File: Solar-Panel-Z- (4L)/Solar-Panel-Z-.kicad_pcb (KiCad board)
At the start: 4 copper layers, 48.4 x 48.4 mm, 89 parts, among them J1 FTS-105-01-X-DV-A, J2 U.FL-R-SMT-1, Q1 NX3008NBKS, Q2 MBT2222ADW1T1, Q3 NX3008NBKS, Q4 MBT2222ADW1T1, Q5 IRLML2803, Q6 IRF7404, U1 BQ25570RGRR, U2 OPT3001, U3 ATB2012-50011-T000, U4 MAX40200AUK

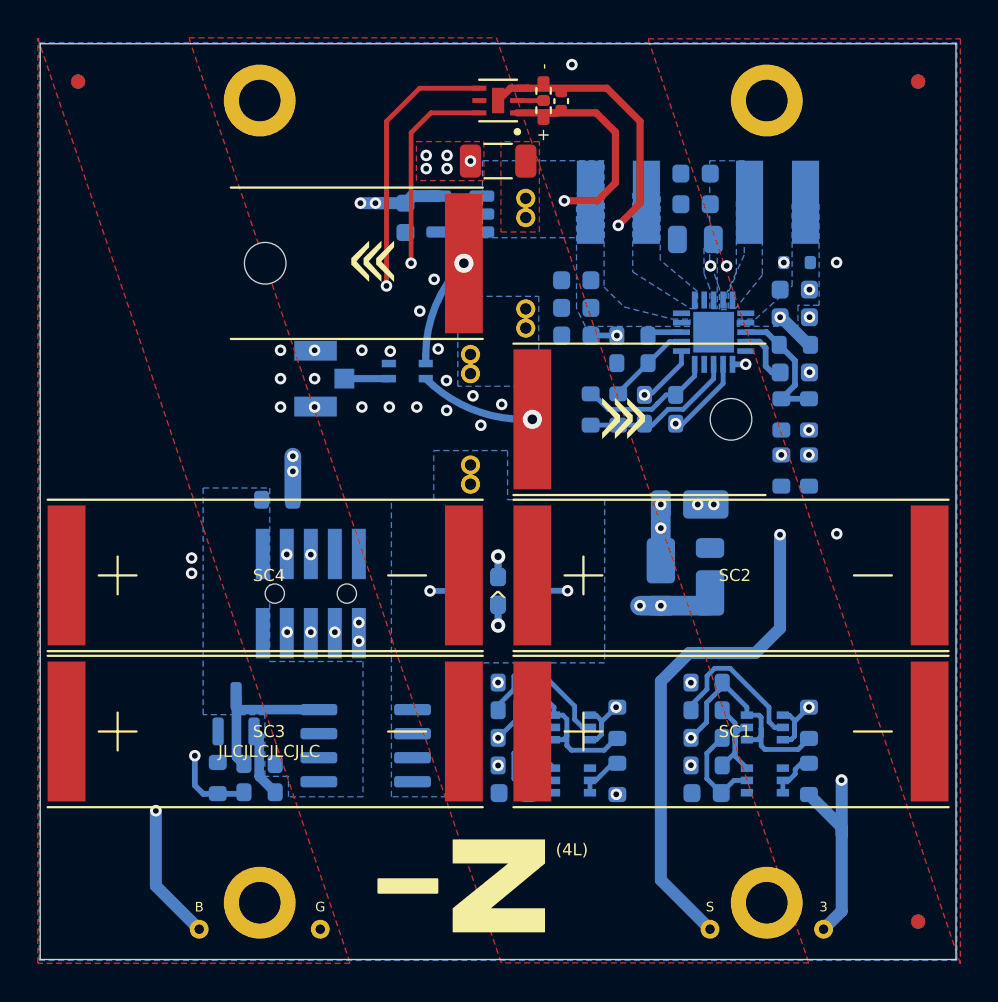
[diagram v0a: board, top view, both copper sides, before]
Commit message: Updated Mounting Holes
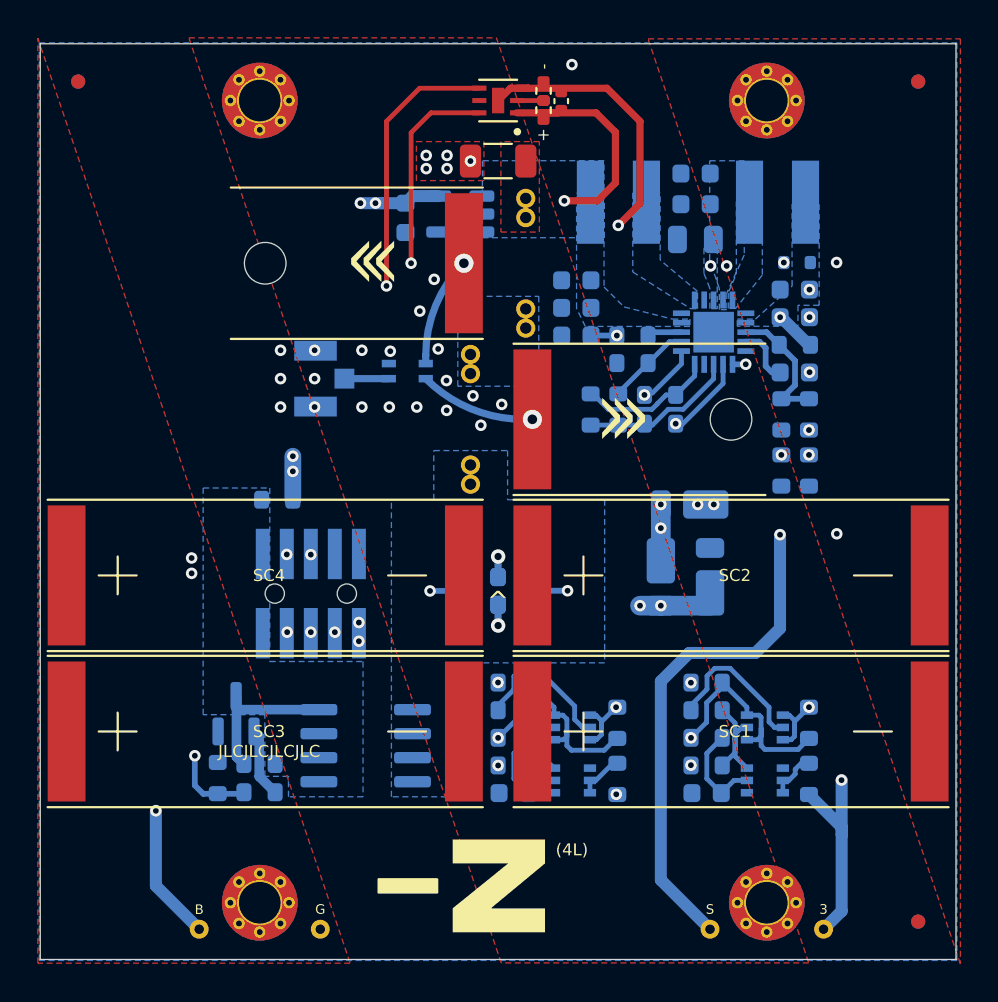
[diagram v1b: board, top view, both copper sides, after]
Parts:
- H1, H2, H3, H4: footprint MountingHole:MountingHole_2.2mm_M2_DIN965_Pad -> solarpanels:MountingHole_2.2mm_M2_DIN965_Pad_TopBottom; moved to F.Cu
- turned H1 to 0 degrees
- turned H2 to 0 degrees
- turned H3 to 0 degrees
- turned H4 to 0 degrees

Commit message: B3/02 Updates
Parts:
- C1: value 1uF -> 0.1uF
- JP1, JP2: moved to F.Cu
- turned JP1 to 180 degrees
- turned JP2 to 180 degrees
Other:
- board text added: "Rev B3/02"
- board text removed: "Rev B3/01"

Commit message: Minor Fixes
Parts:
- JP1: value BurnWire 1 -> BurnWire
- JP2: value BurnWire 2 -> BurnWire
- renumbered U3 to BA1, R32 to R31, R33 to R32, R34 to R33, R35 to R34, U4 to U3
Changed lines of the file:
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@@
   (net 34 "Net-(Q2A-B1)")
   (net 35 "VBAT")
-  (net 36 "Net-(H5-Pad1)")
-  (net 37 "Net-(H6-Pad1)")
+  (net 36 "Net-(BA1-Pad3)")
+  (net 37 "Net-(BA1-Pad4)")
   (net 38 "Net-(Q3A-G2)")
   (net 39 "/VBURN")
@@
   (net 44 "Net-(U2-ADDR)")
   (net 45 "unconnected-(U2-INT-Pad5)")
-  (net 46 "unconnected-(U4-NC-Pad4)")
+  (net 46 "unconnected-(U3-NC-Pad4)")
   (net 47 "Net-(JP2-Pad2)")
   (footprint "solarpanels:KXOB25-05X3F" (layer "F.Cu")
@@
     (property "ki_keywords" "R res resistor")
     (attr smd)
-    (fp_text reference "R35" (at 0 -1.82) (layer "F.SilkS") hide
+    (fp_text reference "R34" (at 0 -1.82) (layer "F.SilkS") hide
         (effects (font (size 1 1) (thickness 0.15)))
     )
@@
         (effects (font (size 0.635 0.635) (thickness 0.1016)))
     )
-    (fp_text value "BurnWire 1" (at 0 4.826) (layer "F.Fab")
+    (fp_text value "BurnWire" (at 0 4.826) (layer "F.Fab")
         (effects (font (size 0.635 0.635) (thickness 0.1016)))
     )
@@
         (effects (font (size 0.635 0.635) (thickness 0.1016)))
     )
-    (fp_text value "BurnWire 2" (at 0 4.826) (layer "F.Fab")
+    (fp_text value "BurnWire" (at 0 4.826) (layer "F.Fab")
         (effects (font (size 0.635 0.635) (thickness 0.1016)))
     )
@@
     (pad "" np_thru_hole circle (at 10.5 0 180) (size 2.2 2.2) (drill 2.2) (layers "F&B.Cu" "*.Mask"))
     (pad "1" smd rect (at 0 0 180) (size 2 7.4) (layers "F.Cu" "F.Paste" "F.Mask")
-      (net 37 "Net-(H6-Pad1)") (pinfunction "1") (pintype "input"))
+      (net 36 "Net-(BA1-Pad3)") (pinfunction "1") (pintype "input"))
   )
   (footprint "Fiducial:Fiducial_0.75mm_Mask1.5mm" (layer "F.Cu")
@@
     (pad "" np_thru_hole circle (at 10.5 0) (size 2.2 2.2) (drill 2.2) (layers "F&B.Cu" "*.Mask"))
     (pad "1" smd rect (at 0 0) (size 2 7.4) (layers "F.Cu" "F.Paste" "F.Mask")
-      (net 36 "Net-(H5-Pad1)") (pinfunction "1") (pintype "input"))
+      (net 37 "Net-(BA1-Pad4)") (pinfunction "1") (pintype "input"))
   )
   (footprint "solarpanels:OPT3001" (layer "F.Cu")
@@
     (property "ki_keywords" "balun rf transformer")
     (attr smd)
-    (fp_text reference "U3" (at 0 0 unlocked) (layer "B.SilkS")
+    (fp_text reference "BA1" (at 0 0 unlocked) (layer "B.SilkS")
         (effects (font (size 0.381 0.381) (thickness 0.0762)) (justify mirror))
     )
@@
       (net 1 "GND") (pinfunction "GND") (pintype "power_in"))
     (pad "3" smd rect (at 0.975 -0.4) (size 0.75 0.4) (layers "B.Cu" "B.Paste" "B.Mask")
-      (net 37 "Net-(H6-Pad1)") (pintype "passive"))
+      (net 36 "Net-(BA1-Pad3)") (pintype "passive"))
     (pad "4" smd rect (at 0.975 0.4) (size 0.75 0.4) (layers "B.Cu" "B.Paste" "B.Mask")
-      (net 36 "Net-(H5-Pad1)") (pintype "passive"))
+      (net 37 "Net-(BA1-Pad4)") (pintype "passive"))
     (model "${KIPRJMOD}/../kicad-libs/3d/ATB2012-50011-T000.stp"
       (offset (xyz 0 0 0))
@@
     (property "ki_keywords" "R res resistor")
     (attr smd)
-    (fp_text reference "R32" (at 0 -1.26 90) (layer "B.SilkS")
+    (fp_text reference "R31" (at 0 -1.26 90) (layer "B.SilkS")
         (effects (font (size 0.508 0.508) (thickness 0.1016)) (justify mirror))
     )
@@
     (property "ki_keywords" "R res resistor")
     (attr smd)
-    (fp_text reference "R34" (at 1.21 -1.57 90) (layer "B.SilkS")
+    (fp_text reference "R33" (at 1.21 -1.57 90) (layer "B.SilkS")
         (effects (font (size 0.508 0.508) (thickness 0.1016) bold) (justify mirror))
     )
@@
     (property "ki_keywords" "R res resistor")
     (attr smd)
-    (fp_text reference "R33" (at 0 -1.27 180) (layer "B.SilkS")
+    (fp_text reference "R32" (at 0 -1.27 180) (layer "B.SilkS")
         (effects (font (size 0.508 0.508) (thickness 0.1016)) (justify mirror))
     )
@@
     (property "ki_keywords" "current switch")
     (attr smd)
-    (fp_text reference "U4" (at 0 -2.2) (layer "B.SilkS")
+    (fp_text reference "U3" (at 0 -2.2) (layer "B.SilkS")
         (effects (font (size 0.508 0.508) (thickness 0.1016)) (justify mirror))
     )
@@
       (net 43 "Net-(U1-VOUT)") (pinfunction "EN") (pintype "input"))
     (pad "4" smd roundrect (at 1.1375 -0.95 180) (size 1.325 0.6) (layers "B.Cu" "B.Paste" "B.Mask") (roundrect_rratio 0.25)
-      (net 46 "unconnected-(U4-NC-Pad4)") (pinfunction "NC") (pintype "no_connect"))
+      (net 46 "unconnected-(U3-NC-Pad4)") (pinfunction "NC") (pintype "no_connect"))
     (pad "5" smd roundrect (at 1.1375 0.95 180) (size 1.325 0.6) (layers "B.Cu" "B.Paste" "B.Mask") (roundrect_rratio 0.25)
       (net 2 "+3V3") (pinfunction "OUT") (pintype "passive"))
@@
   (segment (start 88.61 82.84) (end 88.61 86.81) (width 0.635) (layer "B.Cu") (net 35))
   (segment (start 88.61 86.81) (end 90.9 89.1) (width 0.635) (layer "B.Cu") (net 35))
-  (via (at 108.51 62.15) (size 1.016) (drill 0.508) (layers "F.Cu" "B.Cu") (net 36))
-  (segment (start 108.065539 62.15) (end 108.51 62.15) (width 0.381) (layer "B.Cu") (net 36))
-  (arc (start 102.875 60) (mid 105.256448 61.591237) (end 108.065539 62.15) (width 0.381) (layer "B.Cu") (net 36))
-  (via (at 104.89 53.9) (size 1.016) (drill 0.508) (layers "F.Cu" "B.Cu") (net 37))
-  (segment (start 102.875 59.2) (end 102.875 58.764619) (width 0.381) (layer "B.Cu") (net 37))
-  (arc (start 102.875 58.764619) (mid 103.398677 56.131914) (end 104.89 53.9) (width 0.381) (layer "B.Cu") (net 37))
+  (via (at 104.89 53.9) (size 1.016) (drill 0.508) (layers "F.Cu" "B.Cu") (net 36))
+  (segment (start 102.875 59.2) (end 102.875 58.764619) (width 0.381) (layer "B.Cu") (net 36))
+  (arc (start 102.875 58.764619) (mid 103.398677 56.131914) (end 104.89 53.9) (width 0.381) (layer "B.Cu") (net 36))
+  (via (at 108.51 62.15) (size 1.016) (drill 0.508) (layers "F.Cu" "B.Cu") (net 37))
+  (segment (start 108.065539 62.15) (end 108.51 62.15) (width 0.381) (layer "B.Cu") (net 37))
+  (arc (start 102.875 60) (mid 105.256448 61.591237) (end 108.065539 62.15) (width 0.381) (layer "B.Cu") (net 37))
   (segment (start 111.555 81.235) (end 111.865 81.235) (width 0.254) (layer "B.Cu") (net 38))
   (segment (start 111.865 81.235) (end 112.77 80.33) (width 0.254) (layer "B.Cu") (net 38))

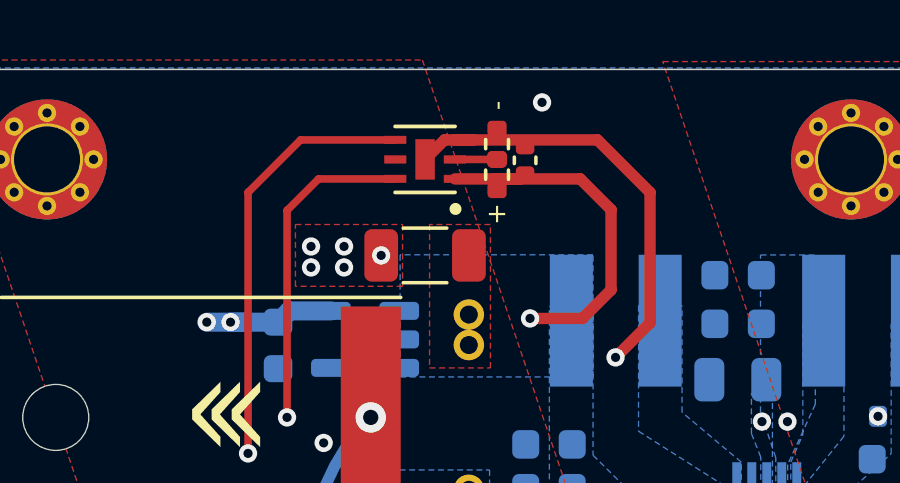
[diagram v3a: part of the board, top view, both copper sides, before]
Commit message: Updated Sun Sensor to OPT4001
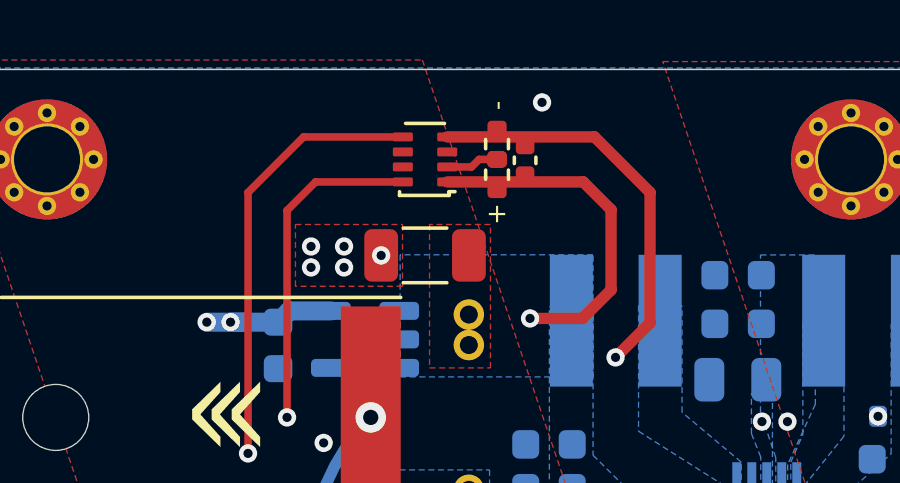
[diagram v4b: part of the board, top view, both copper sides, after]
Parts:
- U2: value OPT3001 -> OPT4001; footprint solarpanels:OPT3001 -> Package_TO_SOT_SMD:SOT-583-8
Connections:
- U2 pad 3: GND -> unconnected-(U2-NC-Pad3)
- U2 pad 4: SCL_LS -> GND
- U2 pad 5: unconnected-(U2-INT-Pad5) -> SCL_LS
- U2 pad 6: SDA_LS -> unconnected-(U2-NC-Pad6)
- U2 pad 7: GND -> unconnected-(U2-INT-Pad7)
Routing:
- net GND: track 15.1 -> 13.5 mm
- net +3V3: track 28.3 -> 27.6 mm

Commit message: Updated Rev to B3/03
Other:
- board text added: "Rev B3/03"
- board text removed: "Rev B3/02"
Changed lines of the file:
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@@
     (effects (font (size 1 1) (thickness 0.15)))
   )
-  (gr_text "Rev B3/02" (at 106.4 46.715) (layer "B.Mask")
+  (gr_text "Rev B3/03" (at 106.4 46.715) (layer "B.Mask")
     (effects (font (size 0.635 0.635) (thickness 0.1524)) (justify mirror))
   )
